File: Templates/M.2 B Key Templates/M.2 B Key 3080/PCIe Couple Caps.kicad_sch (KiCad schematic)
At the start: 2 parts

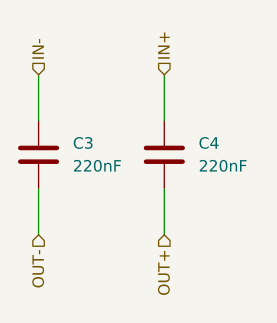
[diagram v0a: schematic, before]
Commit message: Added B Key Templates
-added B key Templates for all sizes
-corrected B key symbol pinout
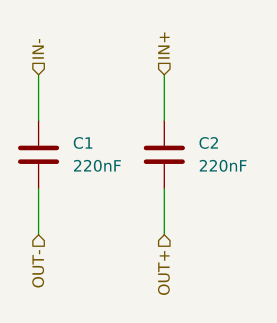
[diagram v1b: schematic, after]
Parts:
- renumbered C3 to C1, C4 to C2
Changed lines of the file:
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@@
 		(dnp no)
 		(fields_autoplaced yes)
-		(property "Reference" "C?"
+		(property "Reference" "C1"
 			(at 133.35 99.0599 0)
 			(effects
@@
 		)
 		(instances
-			(project "M.2 A Key 2230"
-				(path "/540e8a72-89ee-4807-aaa2-5d6c6cec308d/6a934661-433b-4364-b7d9-86a36dc44459/424c4cf5-3c3c-49ef-81c3-66eb0f823d39"
+			(project "M.2 B Key 3080"
+				(path "/3fc86546-8ad2-48b2-92bb-e2164bf7d27c/f934b0d0-e4ed-489f-9ab0-a6c261c4c561/27d77bf0-8499-4672-87f1-05095c3d0a68"
 					(reference "C3")
 					(unit 1)
 				)
-				(path "/540e8a72-89ee-4807-aaa2-5d6c6cec308d/6a934661-433b-4364-b7d9-86a36dc44459/adcd4998-a306-4f2e-b87b-352712eb899b"
-					(reference "C2")
-					(unit 1)
-				)
-			)
-			(project "M.2 A Key"
-				(path "/d21209cf-d1f8-4eb7-aed8-e43843eefa7b/424c4cf5-3c3c-49ef-81c3-66eb0f823d39"
-					(reference "C?")
-					(unit 1)
-				)
-				(path "/d21209cf-d1f8-4eb7-aed8-e43843eefa7b/adcd4998-a306-4f2e-b87b-352712eb899b"
-					(reference "C?")
+				(path "/3fc86546-8ad2-48b2-92bb-e2164bf7d27c/f934b0d0-e4ed-489f-9ab0-a6c261c4c561/2cd6dc77-f114-44b1-9704-d60d213c1d42"
+					(reference "C1")
 					(unit 1)
 				)
@@
 		(dnp no)
 		(fields_autoplaced yes)
-		(property "Reference" "C?"
+		(property "Reference" "C2"
 			(at 147.32 99.0599 0)
 			(effects
@@
 		)
 		(instances
-			(project "M.2 A Key 2230"
-				(path "/540e8a72-89ee-4807-aaa2-5d6c6cec308d/6a934661-433b-4364-b7d9-86a36dc44459/424c4cf5-3c3c-49ef-81c3-66eb0f823d39"
+			(project "M.2 B Key 3080"
+				(path "/3fc86546-8ad2-48b2-92bb-e2164bf7d27c/f934b0d0-e4ed-489f-9ab0-a6c261c4c561/27d77bf0-8499-4672-87f1-05095c3d0a68"
 					(reference "C4")
 					(unit 1)
 				)
-				(path "/540e8a72-89ee-4807-aaa2-5d6c6cec308d/6a934661-433b-4364-b7d9-86a36dc44459/adcd4998-a306-4f2e-b87b-352712eb899b"
-					(reference "C1")
+				(path "/3fc86546-8ad2-48b2-92bb-e2164bf7d27c/f934b0d0-e4ed-489f-9ab0-a6c261c4c561/2cd6dc77-f114-44b1-9704-d60d213c1d42"
+					(reference "C2")
 					(unit 1)
 				)
-			)
-			(project "M.2 A Key"
-				(path "/d21209cf-d1f8-4eb7-aed8-e43843eefa7b/424c4cf5-3c3c-49ef-81c3-66eb0f823d39"
-					(reference "C?")
-					(unit 1)
-				)
-				(path "/d21209cf-d1f8-4eb7-aed8-e43843eefa7b/adcd4998-a306-4f2e-b87b-352712eb899b"
-					(reference "C?")
-					(unit 1)
-				)
